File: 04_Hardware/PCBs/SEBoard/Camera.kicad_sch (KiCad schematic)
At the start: 33 parts, among them J13 YXT-BB10-30S-02, U1 SC200EEMNA-E53-UGNDA

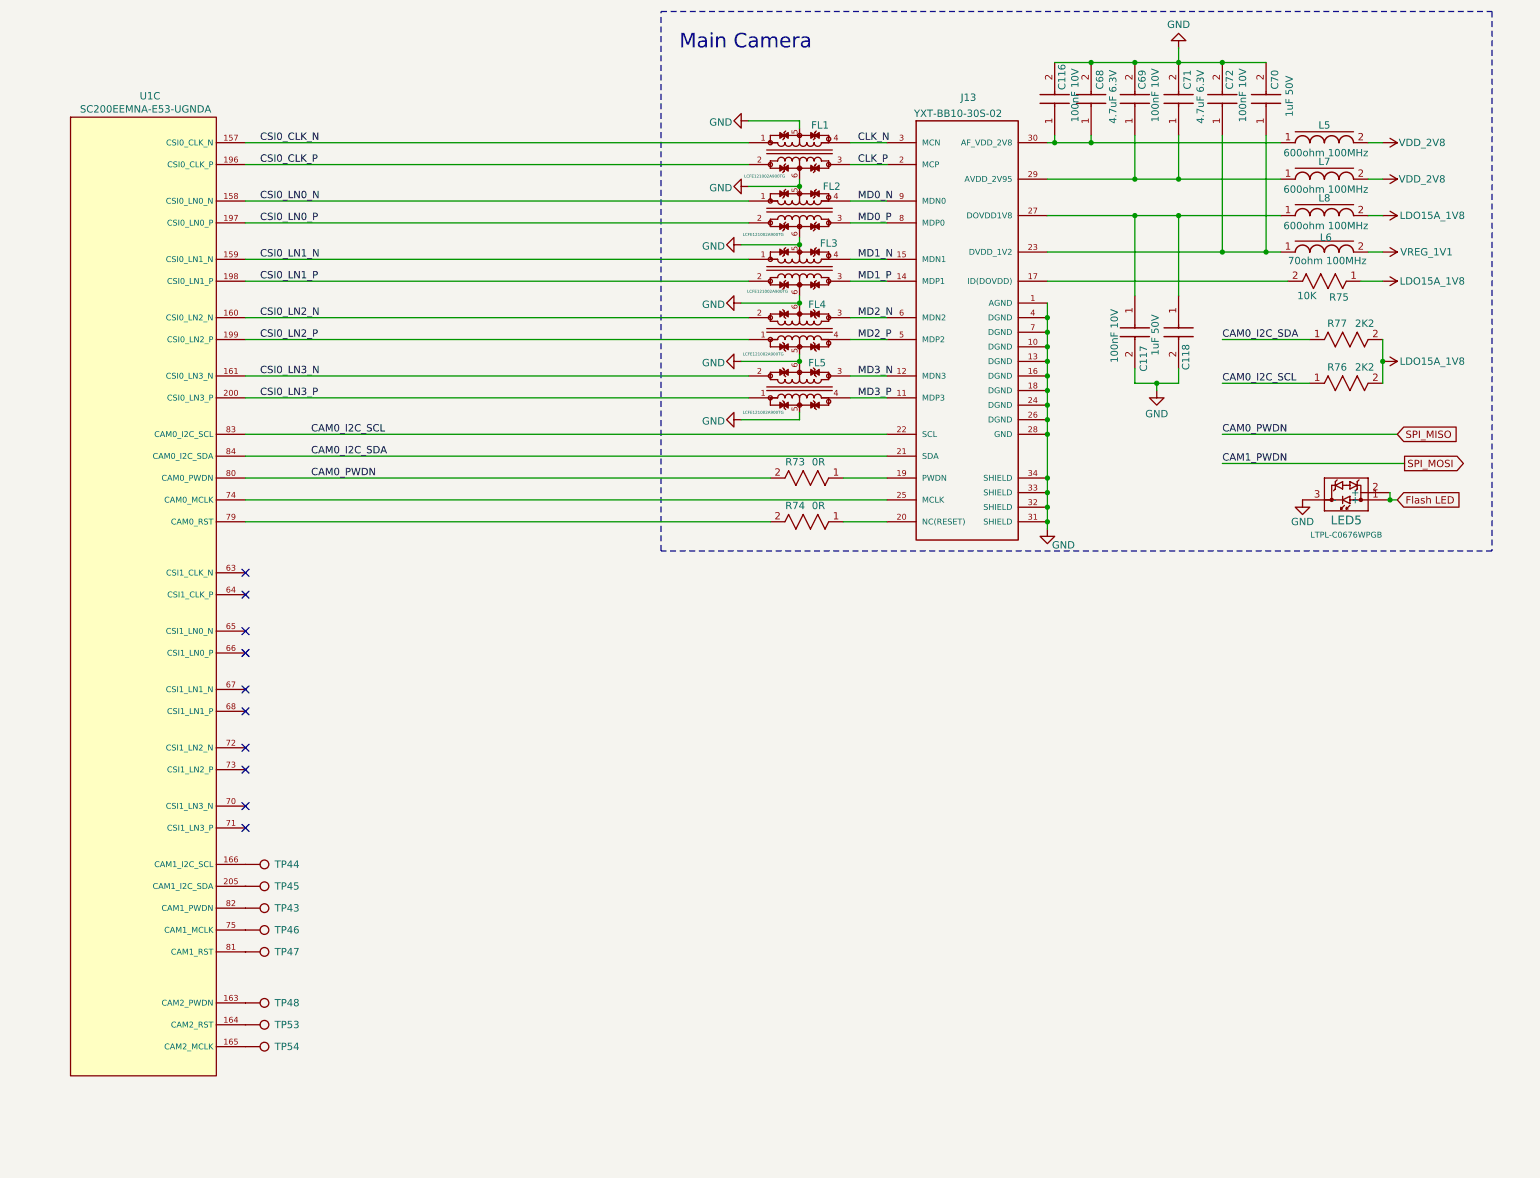
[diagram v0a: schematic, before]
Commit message: feat(schematic): add SE250B4 symbol to schematic (unchecked)
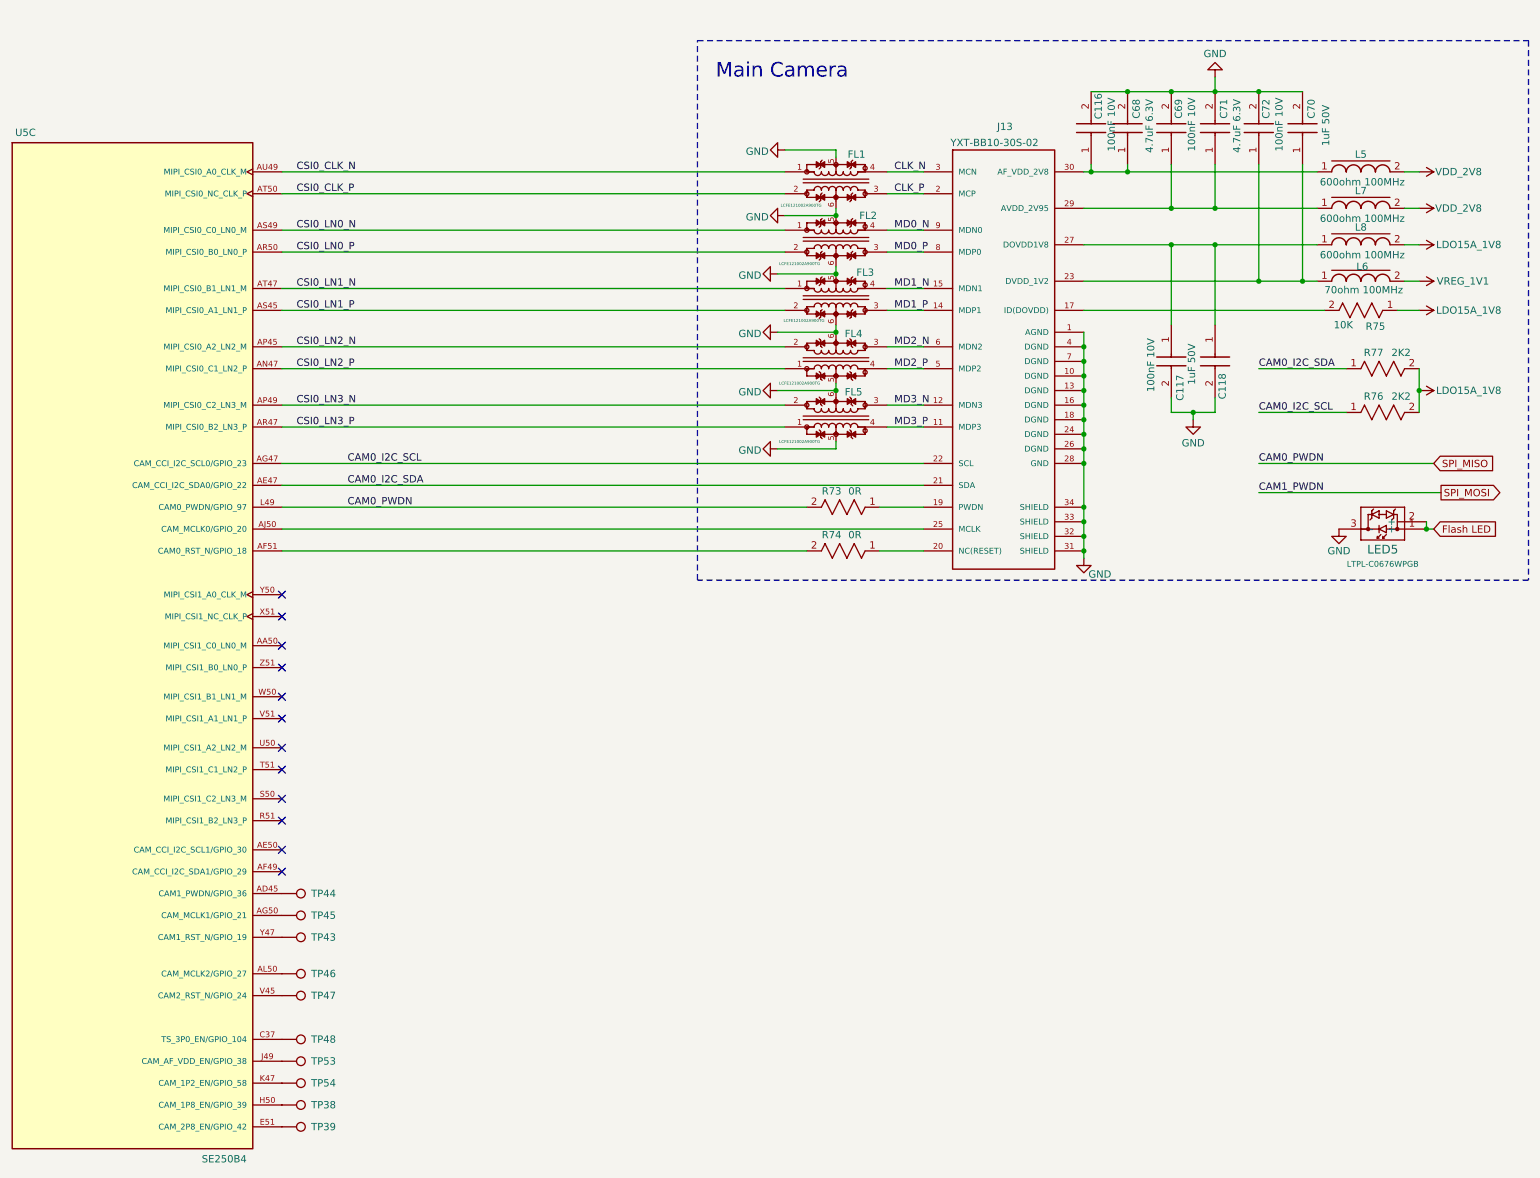
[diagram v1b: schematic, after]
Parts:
- removed U1: SC200EEMNA-E53-UGNDA, SEBoard:SC200E_SC206E, symbol SEBoard:SC200E
- added TP38, TP39: VBAT, TestPoint:TestPoint_Pad_D1.0mm, symbol SEBoard:TestPoint
- added U5: SE250B4, 000MCLib:XCVR_SE250B4-NA, symbol 000MCLib:SE250B4
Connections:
- net CAM0_I2C_SCL: now also U5.AG47 (CAM_CCI_I2C_SCL0/GPIO_23)
- net CAM0_I2C_SDA: now also U5.AE47 (CAM_CCI_I2C_SDA0/GPIO_22)
- net CSI0_CLK_N: now also U5.AU49 (MIPI_CSI0_A0_CLK_M)
- net CSI0_CLK_P: now also U5.AT50 (MIPI_CSI0_NC_CLK_P)
- net CSI0_LN0_N: now also U5.AS49 (MIPI_CSI0_C0_LN0_M)
- net CSI0_LN0_P: now also U5.AR50 (MIPI_CSI0_B0_LN0_P)
- net CSI0_LN1_N: now also U5.AT47 (MIPI_CSI0_B1_LN1_M)
- net CSI0_LN1_P: now also U5.AS45 (MIPI_CSI0_A1_LN1_P)
- net CSI0_LN2_N: now also U5.AP45 (MIPI_CSI0_A2_LN2_M)
- net CSI0_LN2_P: now also U5.AN47 (MIPI_CSI0_C1_LN2_P)
- net CSI0_LN3_N: now also U5.AP49 (MIPI_CSI0_C2_LN3_M)
- net CSI0_LN3_P: now also U5.AR47 (MIPI_CSI0_B2_LN3_P)
- net SPI_MISO: now also U5.L49 (CAM0_PWDN/GPIO_97)
- net at TP45.1: now also U5.AG50 (CAM_MCLK1/GPIO_21)
- net at TP47.1: now also U5.V45 (CAM2_RST_N/GPIO_24)
- net at TP46.1: now also U5.AL50 (CAM_MCLK2/GPIO_27)
- net at TP54.1: now also U5.K47 (CAM_1P2_EN/GPIO_58)
- net at TP53.1: now also U5.J49 (CAM_AF_VDD_EN/GPIO_38)
- net at TP43.1: now also U5.Y47 (CAM1_RST_N/GPIO_19)
- net at J13.25 (MCLK): now also U5.AJ50 (CAM_MCLK0/GPIO_20)
- net at TP44.1: now also U5.AD45 (CAM1_PWDN/GPIO_36)
- net at R74.2: now also U5.AF51 (CAM0_RST_N/GPIO_18)
- net at TP48.1: now also U5.C37 (TS_3P0_EN/GPIO_104)
- new net: TP39.1, U5.E51 (CAM_2P8_EN/GPIO_42)
- new net: TP38.1, U5.H50 (CAM_1P8_EN/GPIO_39)
- no-connect marks 10 -> 12
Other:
- moved on the sheet: C116, C117, C118, C68, C69, C70, C71, C72, FL1, FL2, FL3, FL4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

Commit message: feat: Updated schematic layout and moved new components to Layout
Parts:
- removed TP54: VBAT, TestPoint:TestPoint_Pad_D1.0mm, symbol SEBoard:TestPoint
- C116, C117, C69, C72: footprint SEBoard:CAPC1005X55N -> 000MCLib:CAPC1005X55N; symbol SEBoard:GRM155R71A104KA01D -> 000MCLib:GRM155R71A104KA01D
- C118, C70: footprint SEBoard:CAPC1005X55N -> 000MCLib:CAPC1005X55N; symbol SEBoard:GRM155R61H105KE05D -> 000MCLib:GRM155R61H105KE05D
- C68, C71: footprint SEBoard:CAPC1005X55N -> 000MCLib:CAPC1005X55N; symbol SEBoard:GRM155R60J475ME47D -> 000MCLib:GRM155R60J475ME47D
- FL1, FL2, FL3, FL4, FL5: footprint SEBoard:LCFE121002A900TG -> 000MCLib:LCFE121002A900TG; symbol SEBoard:LCFE121002A900TG -> 000MCLib:LCFE121002A900TG
- J13: footprint SEBoard:YXT_YXT-BB10-30S-02 -> 000MCLib:YXT_YXT-BB10-30S-02; symbol SEBoard:YXT-BB10-30S-02 -> 000MCLib:YXT-BB10-30S-02
- L5, L7, L8: footprint SEBoard:0402 -> 000MCLib:0402; symbol SEBoard:7427927291 -> 000MCLib:7427927291
- L6: footprint SEBoard:0402 -> 000MCLib:0402; symbol SEBoard:7427927370 -> 000MCLib:7427927370
- LED5: footprint SEBoard:LTPL-C0676WPGB -> 000MCLib:LTPL-C0676WPGB; symbol SEBoard:LTPL-C0676WPGB -> 000MCLib:LTPL-C0676WPGB
- R73, R74: footprint SEBoard:RC0402N_YAG -> 000MCLib:RC0402N_YAG; symbol SEBoard:RC0402JR-070RL -> 000MCLib:RC0402JR-070RL
- R75: footprint SEBoard:RC0402N_YAG -> 000MCLib:RC0402N_YAG; symbol SEBoard:RC0402JR-0710KL -> 000MCLib:RC0402JR-0710KL
- R76, R77: footprint SEBoard:RC0402N_YAG -> 000MCLib:RC0402N_YAG; symbol SEBoard:RC0402JR-072K2L -> 000MCLib:RC0402JR-072K2L
- TP38, TP39, TP43, TP44, TP45, TP46, TP47, TP48, TP53: symbol SEBoard:TestPoint -> 000MCLib:TestPoint
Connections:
- net CAM0_1V1_EN: now reaches U5.K47 (CAM_1P2_EN/GPIO_58)
- net SPI_MISO renamed CAM0_PWDN
